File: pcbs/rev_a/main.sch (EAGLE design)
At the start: 12 parts

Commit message: First candidate board
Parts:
- added R4: 2K, resistor:R-US_0309/V
- added R6: 1K, resistor:R-US_0309/V
- R1, R2: value (none) -> 10K
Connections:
- removed net N$34: C1.2, JP1.5, JP2.3, JP3.5, JP5.4, R1.1, U$1.GND, U$7.PB_P0
- new net N$16: C1.2, JP1.5, JP2.3, JP3.5, JP5.1, R1.1, R4.2, U$1.GND, U$7.PB_P0
- new net N$9: JP5.2, R4.1, R6.2
- net N$1: no longer JP5.1
- net N$11: now also R6.1; no longer JP5.2
- net N$2: now also JP5.4

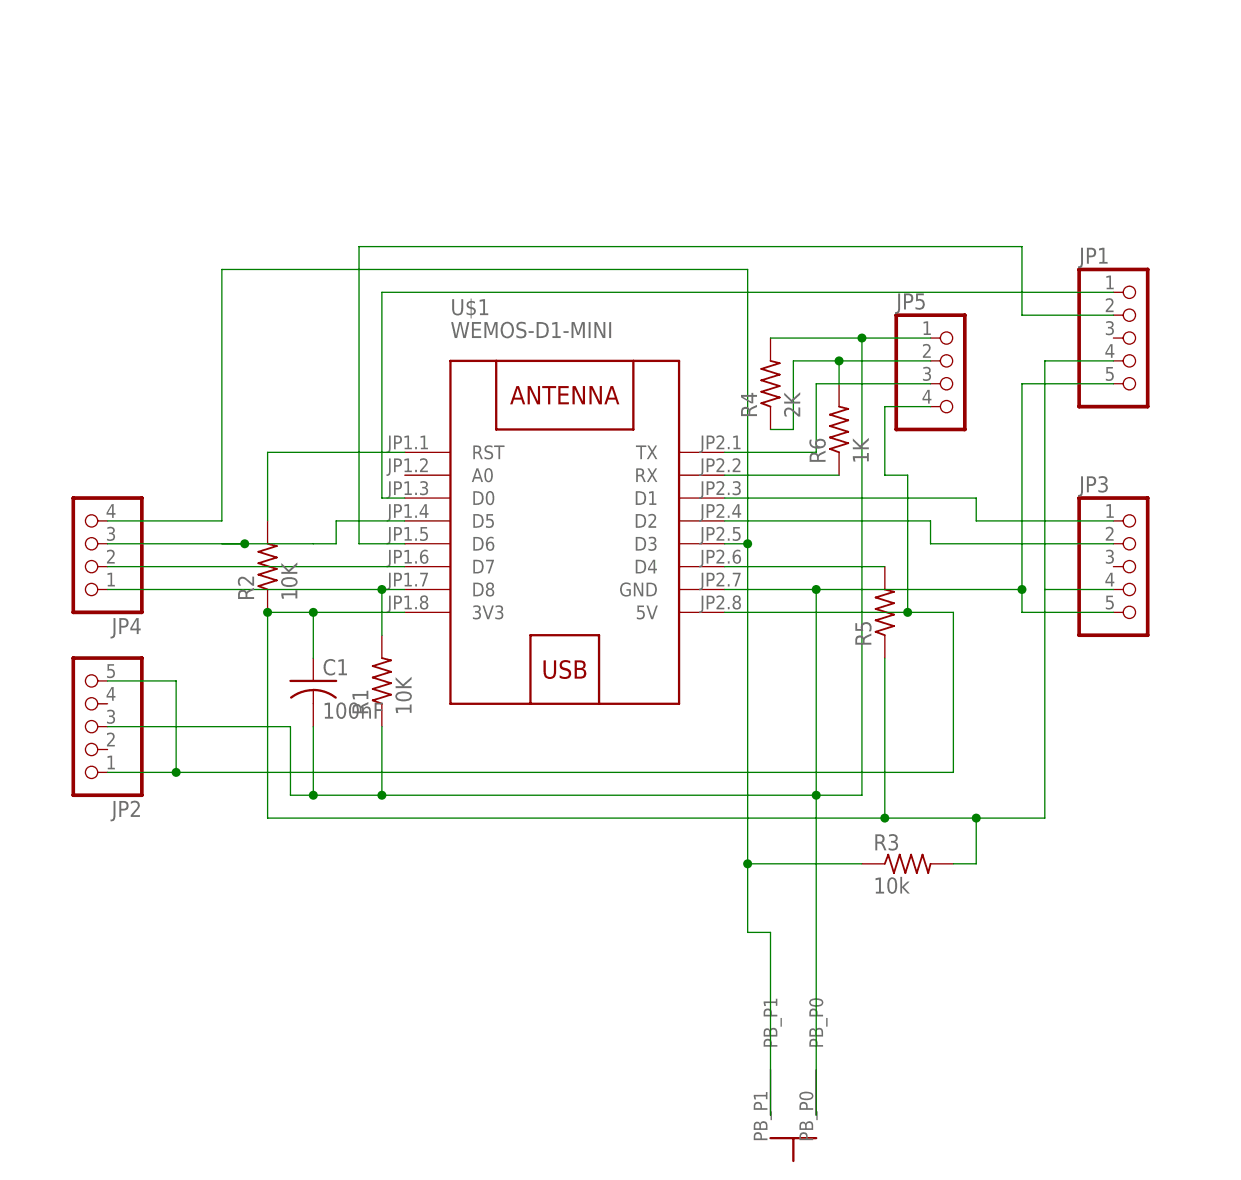
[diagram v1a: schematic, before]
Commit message: Work on PCB and firmware updates for the SR04 range finder - Move PCB pinouts.  I wasn't able to use the TX or RX pins as inputs - Add a WS2812 plug.  It might be usable with the last port, and it does no harm - Work on the firmware for the SR04.  Firmware can not find successfully return ranges.  Reliability still needs work
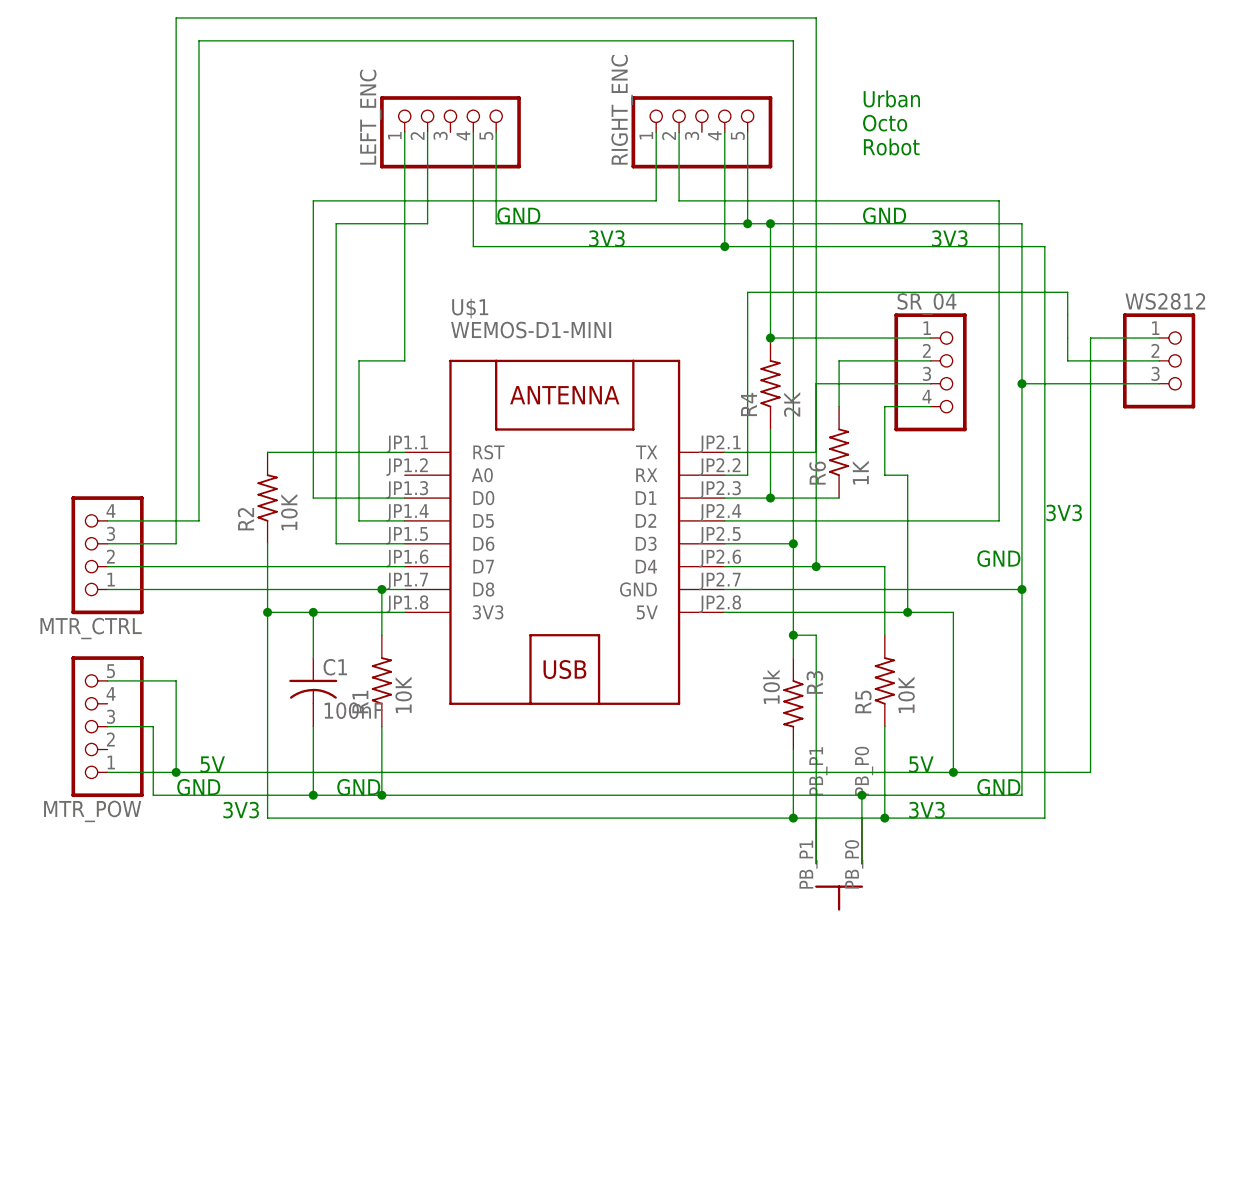
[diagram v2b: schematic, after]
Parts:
- removed JP1, JP3: (no value), pinhead:PINHD-1X5
- added LEFT_ENC, RIGHT_ENC: (no value), pinhead:PINHD-1X5
- added WS2812: (no value), pinhead:PINHD-1X3
- R3: device resistor:R-US_0309/V -> resistor:R-US_0207/2V
- R5: value (none) -> 10K
- renumbered JP2 to MTR_POW, JP4 to MTR_CTRL, JP5 to SR_04
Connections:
- net N$1: now also U$1.RX, WS2812.2; no longer C1.1, JP1.4, JP3.4, R2.1, R3.2, R5.1, U$1.3V3
- net N$11: now also R4.1, U$1.D1; no longer U$1.RX
- net N$13: now also R5.2, U$1.D4; no longer U$1.D5
- net N$16: now also LEFT_ENC.5, RIGHT_ENC.5, WS2812.3; no longer JP1.5, JP3.5
- net N$2: now also WS2812.1
- net N$3: now also LEFT_ENC.1, U$1.D5; no longer JP1.1, U$1.D0
- net N$5: now also RIGHT_ENC.2, U$1.D2; no longer JP3.1, U$1.D1
- net N$6: now also LEFT_ENC.2; no longer JP1.2
- net N$7: now also RIGHT_ENC.1, U$1.D0; no longer JP3.2, U$1.D2
- net N$8: now also C1.1, LEFT_ENC.4, R2.1, R3.2, R5.1, RIGHT_ENC.4, U$1.3V3; no longer R5.2, U$1.D4
- net N$9: no longer R4.1
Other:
- note added: "3V3"
- note added: "5V"
- note added: "GND"
- note added: "Urban Octo Robot"
- moved on the sheet: R2, R3, R5, R6

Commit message: Move GPIOs so the firmware can (hopefully) use interrupts instead of polling in encoders.
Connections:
- net N$4: now also U$1.D0; no longer U$1.D7
- net N$7: now also U$1.D7; no longer U$1.D0
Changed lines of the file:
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@@
-</segment>
-</net>
-<net name="N$4" class="0">
-<segment>
-<pinref part="U$1" gate="G$1" pin="D7"/>
-<pinref part="MTR_CTRL" gate="A" pin="2"/>
-<wire x1="-73.66" y1="45.72" x2="-106.68" y2="45.72" width="0.1524" layer="91"/>
 </segment>
 </net>
@@
 <net name="N$7" class="0">
 <segment>
-<pinref part="U$1" gate="G$1" pin="D0"/>
 <wire x1="-45.72" y1="86.36" x2="-83.82" y2="86.36" width="0.1524" layer="91"/>
-<wire x1="-73.66" y1="53.34" x2="-83.82" y2="53.34" width="0.1524" layer="91"/>
-<wire x1="-83.82" y1="53.34" x2="-83.82" y2="86.36" width="0.1524" layer="91"/>
+<wire x1="-83.82" y1="45.72" x2="-83.82" y2="86.36" width="0.1524" layer="91"/>
 <pinref part="RIGHT_ENC" gate="A" pin="1"/>
 <wire x1="-45.72" y1="93.98" x2="-45.72" y2="86.36" width="0.1524" layer="91"/>
+<pinref part="U$1" gate="G$1" pin="D7"/>
+<wire x1="-83.82" y1="45.72" x2="-73.66" y2="45.72" width="0.1524" layer="91"/>
 </segment>
 </net>
@@
 </segment>
 </net>
+<net name="N$4" class="0">
+<segment>
+<pinref part="U$1" gate="G$1" pin="D0"/>
+<wire x1="-73.66" y1="53.34" x2="-93.98" y2="53.34" width="0.1524" layer="91"/>
+<pinref part="MTR_CTRL" gate="A" pin="2"/>
+<wire x1="-93.98" y1="53.34" x2="-93.98" y2="45.72" width="0.1524" layer="91"/>
+<wire x1="-93.98" y1="45.72" x2="-106.68" y2="45.72" width="0.1524" layer="91"/>
+</segment>
+</net>
